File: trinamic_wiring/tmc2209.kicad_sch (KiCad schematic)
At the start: 0 parts

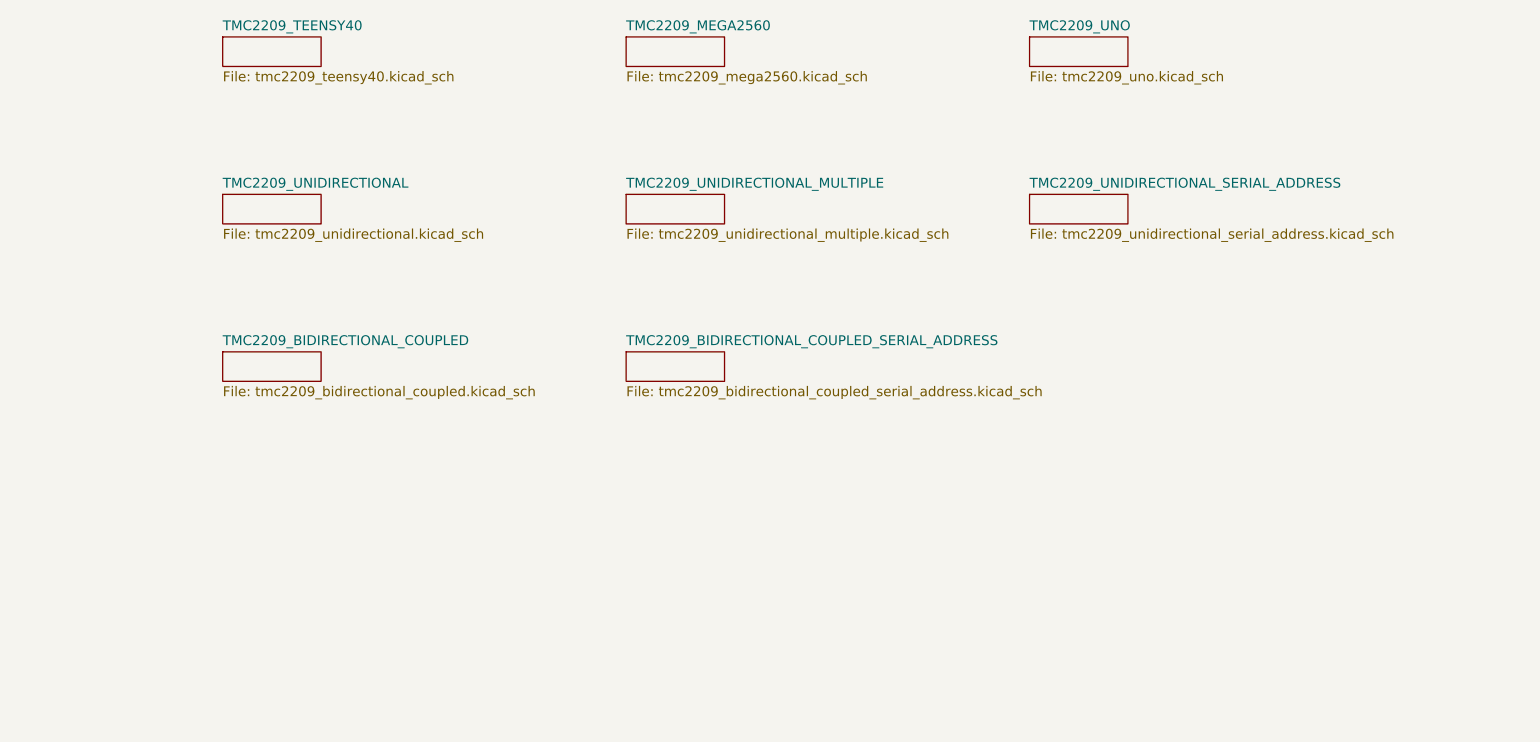
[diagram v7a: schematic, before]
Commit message: Modify svg files
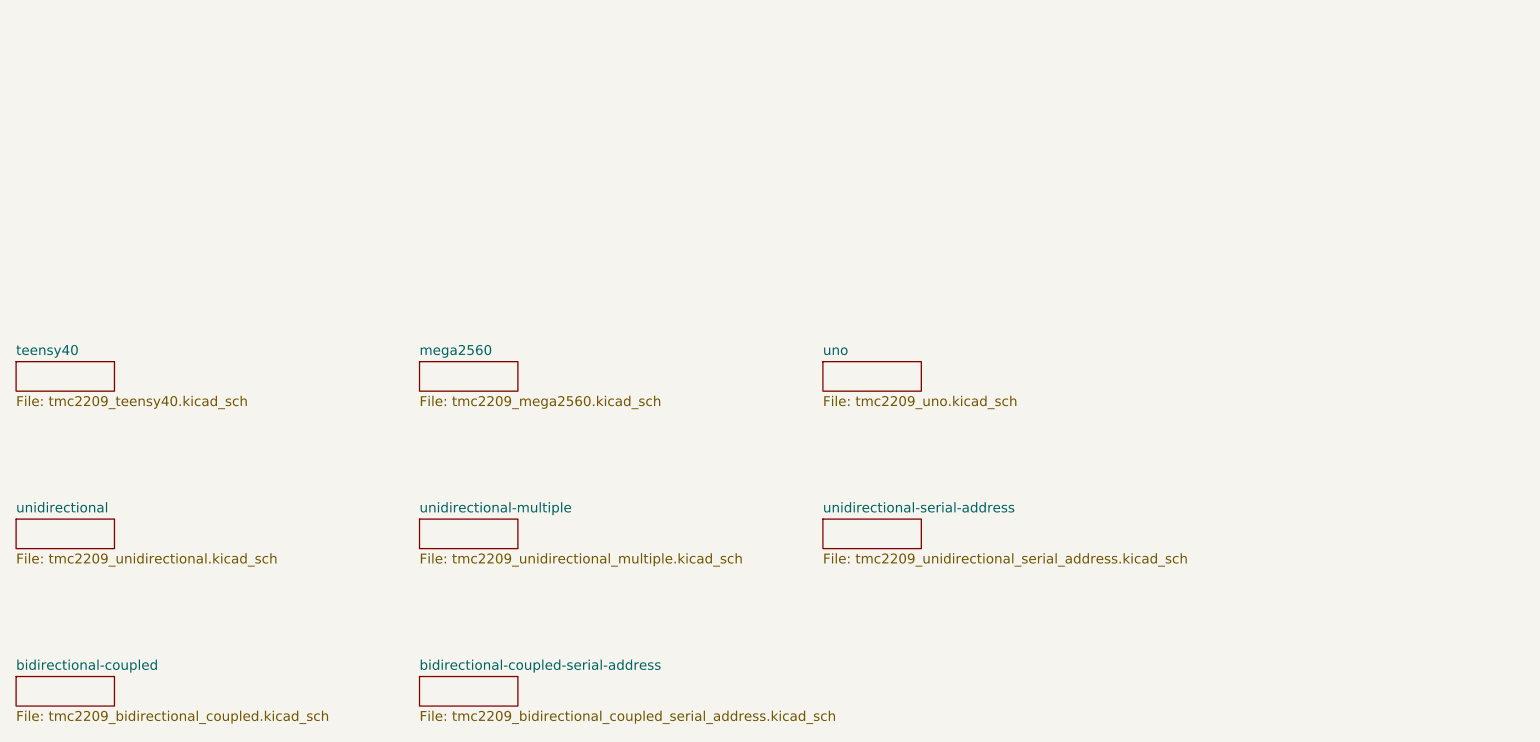
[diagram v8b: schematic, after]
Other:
- sheet TMC2209_BIDIRECTIONAL_COUPLED renamed bidirectional-coupled
- sheet TMC2209_BIDIRECTIONAL_COUPLED_SERIAL_ADDRESS renamed bidirectional-coupled-serial-address
- sheet TMC2209_MEGA2560 renamed mega2560
- sheet TMC2209_TEENSY40 renamed teensy40
- sheet TMC2209_UNIDIRECTIONAL renamed unidirectional
- sheet TMC2209_UNIDIRECTIONAL_MULTIPLE renamed unidirectional-multiple
- sheet TMC2209_UNIDIRECTIONAL_SERIAL_ADDRESS renamed unidirectional-serial-address
- sheet TMC2209_UNO renamed uno
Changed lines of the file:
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@@
   (title_block
     (title "Trinamic Wiring")
-    (date "2023-06-27")
-    (rev "0.3")
+    (date "2023-08-01")
+    (rev "0.4")
     (company "Janelia Research Campus")
   )
-  (sheet (at 100.33 55.88) (size 12.7 3.81) (fields_autoplaced)
+  (sheet (at 73.66 97.79) (size 12.7 3.81) (fields_autoplaced)
     (stroke (width 0.1524) (type solid))
     (fill (color 0 0 0 0.0000))
-    (property "Sheetname" "TMC2209_UNIDIRECTIONAL" (at 100.33 55.1684 0)
+    (property "Sheetname" "unidirectional" (at 73.66 97.0784 0)
       (effects (font (size 1.27 1.27)) (justify left bottom))
     )
-    (property "Sheetfile" "tmc2209_unidirectional.kicad_sch" (at 100.33 60.2746 0)
+    (property "Sheetfile" "tmc2209_unidirectional.kicad_sch" (at 73.66 102.1846 0)
       (effects (font (size 1.27 1.27)) (justify left top))
     )
@@
     )
   )
-  (sheet (at 100.33 35.56) (size 12.7 3.81) (fields_autoplaced)
+  (sheet (at 73.66 77.47) (size 12.7 3.81) (fields_autoplaced)
     (stroke (width 0.1524) (type solid))
     (fill (color 0 0 0 0.0000))
-    (property "Sheetname" "TMC2209_TEENSY40" (at 100.33 34.8484 0)
+    (property "Sheetname" "teensy40" (at 73.66 76.7584 0)
       (effects (font (size 1.27 1.27)) (justify left bottom))
     )
-    (property "Sheetfile" "tmc2209_teensy40.kicad_sch" (at 100.33 39.9546 0)
+    (property "Sheetfile" "tmc2209_teensy40.kicad_sch" (at 73.66 81.8646 0)
       (effects (font (size 1.27 1.27)) (justify left top))
     )
@@
     )
   )
-  (sheet (at 152.4 55.88) (size 12.7 3.81) (fields_autoplaced)
+  (sheet (at 125.73 97.79) (size 12.7 3.81) (fields_autoplaced)
     (stroke (width 0.1524) (type solid))
     (fill (color 0 0 0 0.0000))
-    (property "Sheetname" "TMC2209_UNIDIRECTIONAL_MULTIPLE" (at 152.4 55.1684 0)
+    (property "Sheetname" "unidirectional-multiple" (at 125.73 97.0784 0)
       (effects (font (size 1.27 1.27)) (justify left bottom))
     )
-    (property "Sheetfile" "tmc2209_unidirectional_multiple.kicad_sch" (at 152.4 60.2746 0)
+    (property "Sheetfile" "tmc2209_unidirectional_multiple.kicad_sch" (at 125.73 102.1846 0)
       (effects (font (size 1.27 1.27)) (justify left top))
     )
@@
     )
   )
-  (sheet (at 152.4 76.2) (size 12.7 3.81) (fields_autoplaced)
+  (sheet (at 125.73 118.11) (size 12.7 3.81) (fields_autoplaced)
     (stroke (width 0.1524) (type solid))
     (fill (color 0 0 0 0.0000))
-    (property "Sheetname" "TMC2209_BIDIRECTIONAL_COUPLED_SERIAL_ADDRESS" (at 152.4 75.4884 0)
+    (property "Sheetname" "bidirectional-coupled-serial-address" (at 125.73 117.3984 0)
       (effects (font (size 1.27 1.27)) (justify left bottom))
     )
-    (property "Sheetfile" "tmc2209_bidirectional_coupled_serial_address.kicad_sch" (at 152.4 80.5946 0)
+    (property "Sheetfile" "tmc2209_bidirectional_coupled_serial_address.kicad_sch" (at 125.73 122.5046 0)
       (effects (font (size 1.27 1.27)) (justify left top))
     )
@@
     )
   )
-  (sheet (at 204.47 35.56) (size 12.7 3.81) (fields_autoplaced)
+  (sheet (at 177.8 77.47) (size 12.7 3.81) (fields_autoplaced)
     (stroke (width 0.1524) (type solid))
     (fill (color 0 0 0 0.0000))
-    (property "Sheetname" "TMC2209_UNO" (at 204.47 34.8484 0)
+    (property "Sheetname" "uno" (at 177.8 76.7584 0)
       (effects (font (size 1.27 1.27)) (justify left bottom))
     )
-    (property "Sheetfile" "tmc2209_uno.kicad_sch" (at 204.47 39.9546 0)
+    (property "Sheetfile" "tmc2209_uno.kicad_sch" (at 177.8 81.8646 0)
       (effects (font (size 1.27 1.27)) (justify left top))
     )
@@
     )
   )
-  (sheet (at 204.47 55.88) (size 12.7 3.81) (fields_autoplaced)
+  (sheet (at 177.8 97.79) (size 12.7 3.81) (fields_autoplaced)
     (stroke (width 0.1524) (type solid))
     (fill (color 0 0 0 0.0000))
-    (property "Sheetname" "TMC2209_UNIDIRECTIONAL_SERIAL_ADDRESS" (at 204.47 55.1684 0)
+    (property "Sheetname" "unidirectional-serial-address" (at 177.8 97.0784 0)
       (effects (font (size 1.27 1.27)) (justify left bottom))
     )
-    (property "Sheetfile" "tmc2209_unidirectional_serial_address.kicad_sch" (at 204.47 60.2746 0)
+    (property "Sheetfile" "tmc2209_unidirectional_serial_address.kicad_sch" (at 177.8 102.1846 0)
       (effects (font (size 1.27 1.27)) (justify left top))
     )
@@
     )
   )
-  (sheet (at 100.33 76.2) (size 12.7 3.81) (fields_autoplaced)
+  (sheet (at 73.66 118.11) (size 12.7 3.81) (fields_autoplaced)
     (stroke (width 0.1524) (type solid))
     (fill (color 0 0 0 0.0000))
-    (property "Sheetname" "TMC2209_BIDIRECTIONAL_COUPLED" (at 100.33 75.4884 0)
+    (property "Sheetname" "bidirectional-coupled" (at 73.66 117.3984 0)
       (effects (font (size 1.27 1.27)) (justify left bottom))
     )
-    (property "Sheetfile" "tmc2209_bidirectional_coupled.kicad_sch" (at 100.33 80.5946 0)
+    (property "Sheetfile" "tmc2209_bidirectional_coupled.kicad_sch" (at 73.66 122.5046 0)
       (effects (font (size 1.27 1.27)) (justify left top))
     )
@@
     )
   )
-  (sheet (at 152.4 35.56) (size 12.7 3.81) (fields_autoplaced)
+  (sheet (at 125.73 77.47) (size 12.7 3.81) (fields_autoplaced)
     (stroke (width 0.1524) (type solid))
     (fill (color 0 0 0 0.0000))
-    (property "Sheetname" "TMC2209_MEGA2560" (at 152.4 34.8484 0)
+    (property "Sheetname" "mega2560" (at 125.73 76.7584 0)
       (effects (font (size 1.27 1.27)) (justify left bottom))
     )
-    (property "Sheetfile" "tmc2209_mega2560.kicad_sch" (at 152.4 39.9546 0)
+    (property "Sheetfile" "tmc2209_mega2560.kicad_sch" (at 125.73 81.8646 0)
       (effects (font (size 1.27 1.27)) (justify left top))
     )
